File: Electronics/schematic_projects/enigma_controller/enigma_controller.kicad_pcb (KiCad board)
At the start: 6 copper layers, 156.7 x 120.8 mm, 92 parts, among them IC1 TPD8S300ARUKR, IC10 MCP23017-E_SO, IC11 RT9742SNGV, IC12 TPD1E05U06DPYT, IC13 ESD224DQAR, IC14 ESD224DQAR, IC2 ESD321DYAR, IC3 ESD321DYAR, IC4 ESD321DYAR, IC5 ESD321DYAR, IC6 ESD321DYAR, IC7 ESD321DYAR, IC8 AP22653W6-7, IC9 MCP23017-E_SO, J1 Conn_02x05_Odd_Even, J10 A70-112-331N126, J11 Conn_02x05_Odd_Even, J12 Conn_01x02, J15 Conn_01x02, J16 Conn_01x02, J17 Conn_01x02, J18 Conn_01x02, J19 Conn_01x02, J2 Conn_02x04_Odd_Even, J20 Conn_01x02, J21 Conn_02x05_Odd_Even, J22 Conn_02x05_Odd_Even, J23 Conn_01x02, J24 Conn_01x02, J25 Conn_01x02, J26 Conn_01x02, J27 Conn_01x02, J3 USB1040-GF-L-B, J4 USB_C_Receptacle_USB2.0_16P, J5 46765-0301, J6 Conn_02x05_Odd_Even, J7 Conn_02x07_Odd_Even, J8 USB3_A_Stacked, J9 Conn_02x07_Odd_Even, M1 Fan_4pin

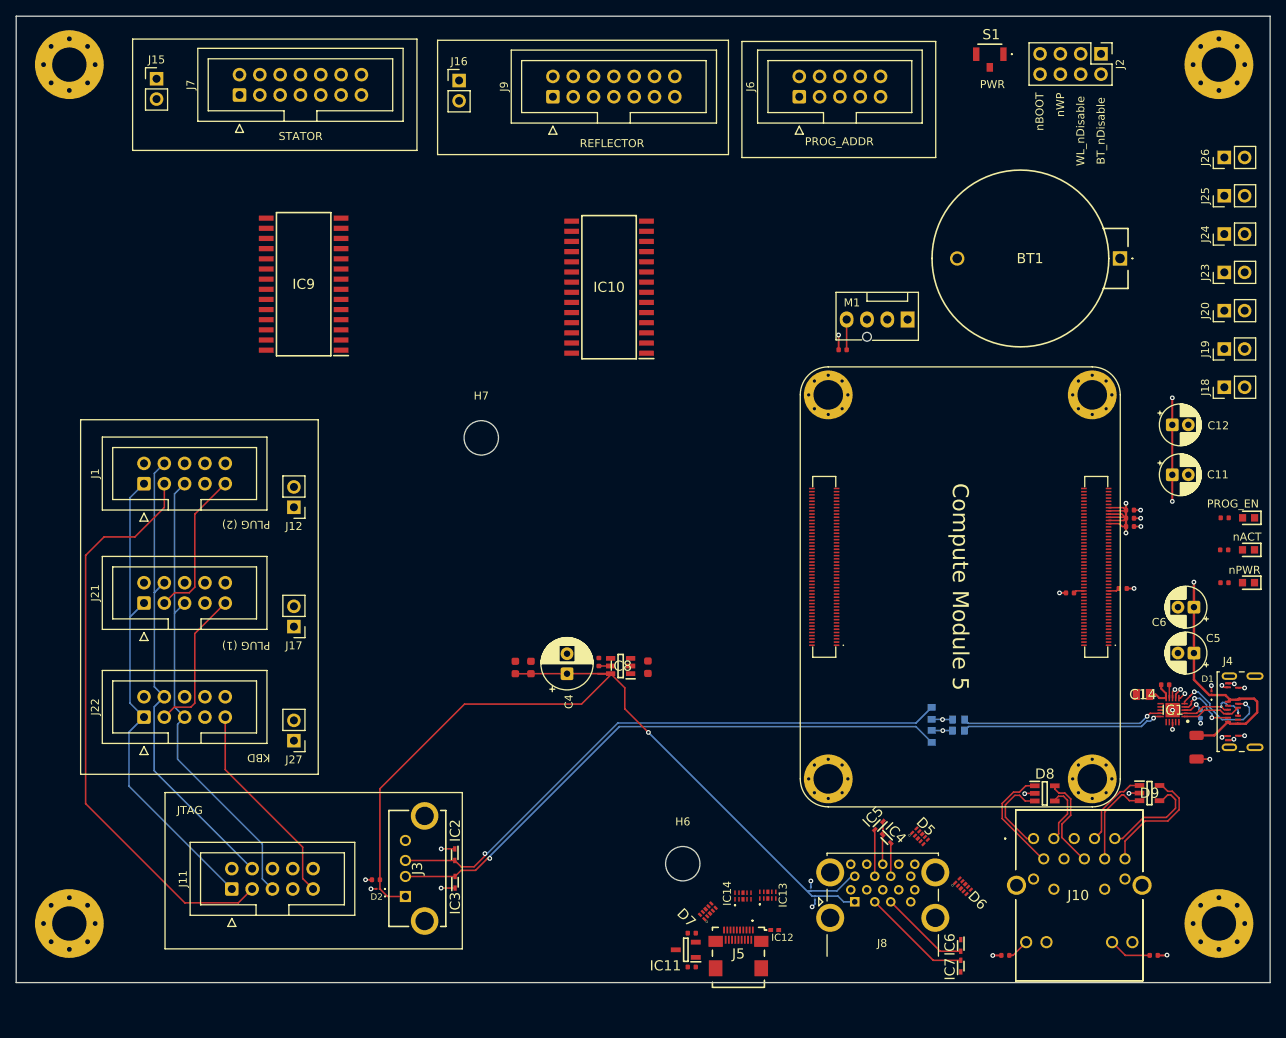
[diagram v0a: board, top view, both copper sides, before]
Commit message: Updated for impedance calculated trace widths.
Also added slow signals and traces for ESD protection components.
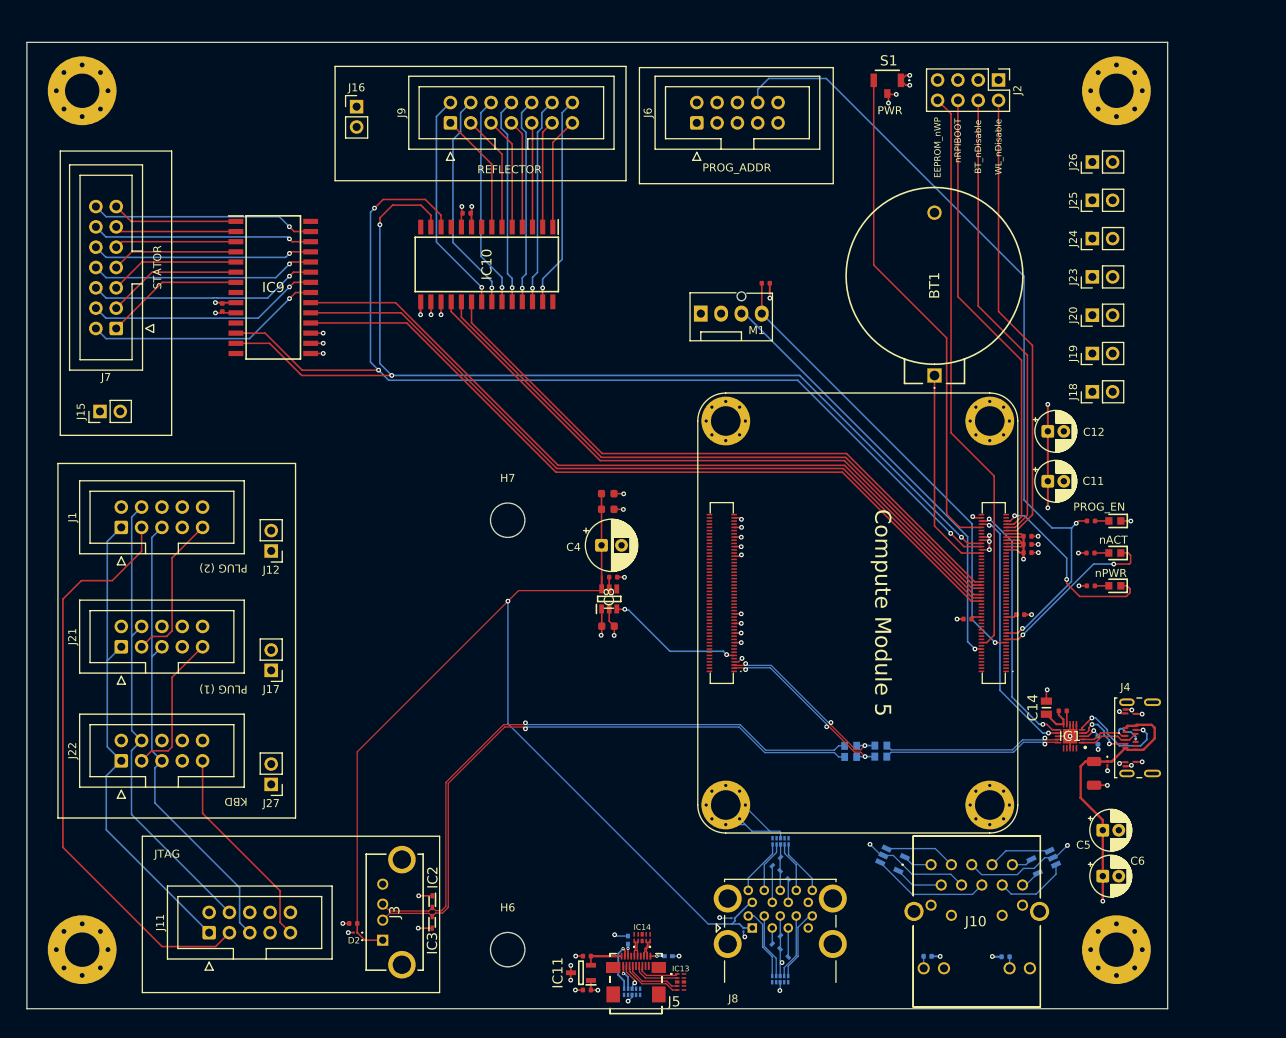
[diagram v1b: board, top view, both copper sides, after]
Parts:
- added C17: 100nF, PCM_JLCPCB:C_0402, F.Cu at (123.8, 54.2)
- added C20: 100nF, PCM_JLCPCB:C_0402, F.Cu at (93.3, 66.0)
- added IC15: TPD1E05U06DPYT, Enigma_Components:TPD1E05U06DPYT, B.Cu at (144.0, 145.1)
- D5, D6, D7, D8, D9, IC12, IC4, IC5, IC6, IC7, R3, R4: moved to B.Cu
- moved J15 42.2 mm to (78.0, 79.0), turned to 90 degrees
- moved C6 35.5 mm to (203.4, 137.1), turned to 0 degrees
- moved J7 33.0 mm to (80.1, 68.7), turned to 180 degrees
- moved BT1 27.4 mm to (182.3, 74.5), turned to -90 degrees
- moved M1 25.9 mm to (153.1, 66.8), turned to 0 degrees
- moved D6 25.6 mm to (163.1, 150.0), turned to 0 degrees
- moved C5 24.9 mm to (203.4, 131.4), turned to 0 degrees
- moved C3 24.6 mm to (141.5, 89.3), turned to 0 degrees
- moved H6 24.4 mm to (129.0, 146.3)
- moved IC7 23.3 mm to (162.6, 145.1), turned to -135 degrees
- moved IC6 22.1 mm to (163.6, 146.7), turned to -45 degrees
- moved C19 22.0 mm to (141.5, 91.2), turned to 0 degrees
- moved D8 20.8 mm to (177.1, 135.1), turned to -25 degrees
- moved R4 18.5 mm to (191.2, 147.2), turned to 180 degrees
- moved D5 17.4 mm to (163.1, 132.8), turned to 180 degrees
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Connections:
- D6 pad 1: /enigma_controller_HS/USB3_0_RX_N -> /enigma_controller_HS/USB3_0_TX_P
- D6 pad 2: /enigma_controller_HS/USB3_0_RX_P -> /enigma_controller_HS/USB3_0_TX_N
- D6 pad 4: /enigma_controller_HS/USB3_0_TX_N -> /enigma_controller_HS/USB3_0_RX_P
- D6 pad 5: /enigma_controller_HS/USB3_0_TX_P -> /enigma_controller_HS/USB3_0_RX_N
- D7 pad 1: /enigma_controller_HS/HDMI0_SDA -> /enigma_controller_HS/HDMI0_SCL
- D7 pad 2: /enigma_controller_HS/HDMI0_SCL -> /enigma_controller_HS/HDMI0_SDA
- D7 pad 4: /enigma_controller_HS/HDMI0_CEC -> unconnected-(D7-D2+-Pad4)
- D7 pad 5: /enigma_controller_HS/HDMI0_UTIL -> unconnected-(D7-D2--Pad5)
- D8 pad 1: /ETH_PAIR0_N -> /ETH_PAIR1_N
- D8 pad 3: /ETH_PAIR0_P -> /ETH_PAIR1_P
- D8 pad 4: /ETH_PAIR1_P -> /ETH_PAIR0_P
- D8 pad 5: /ETH_PAIR1_N -> /ETH_PAIR0_N
- D9 pad 4: /ETH_PAIR3_P -> /ETH_PAIR3_N
- D9 pad 5: /ETH_PAIR3_N -> /ETH_PAIR3_P
- H1 pad 46: /EXP2_INT_B -> /EXP1_nRST
- H1 pad 48: /EXP2_INT_A -> /EXP1_INT_B
- H1 pad 50: /EXP1_INT_B -> /EXP1_INT_A
- H1 pad 54: /EXP1_INT_A -> /EXP2_nRST
- H1 pad 56: /EXP2_nRST -> /EXP2_INT_B
- H1 pad 58: /EXP1_nRST -> /EXP2_INT_A
- IC10 pad 1: /pBIN_IN_B1 -> /pBIN_OUT_nOE_A
- IC10 pad 2: /pBIN_IN_B2 -> /pBIN_OUT_A6
- IC10 pad 21: /pBIN_OUT_B1 -> /pBIN_IN_B1
- IC10 pad 22: /pBIN_OUT_B2 -> /pBIN_IN_B2
- IC10 pad 23: /pBIN_OUT_B3 -> /pBIN_IN_B3
- IC10 pad 24: /pBIN_OUT_B4 -> /pBIN_IN_B4
- IC10 pad 25: /pBIN_OUT_B5 -> /pBIN_IN_B5
- IC10 pad 26: /pBIN_OUT_B6 -> /pBIN_IN_B6
- IC10 pad 27: /pBIN_OUT_nOE_B -> /pBIN_IN_nOE_B
- IC10 pad 3: /pBIN_IN_B3 -> /pBIN_OUT_A5
- IC10 pad 4: /pBIN_IN_B4 -> /pBIN_OUT_A4
- IC10 pad 5: /pBIN_IN_B5 -> /pBIN_OUT_A3
- IC10 pad 6: /pBIN_IN_B6 -> /pBIN_OUT_A2
- IC10 pad 7: /pBIN_IN_nOE_B -> /pBIN_OUT_A1
- IC13 pad 1: /enigma_controller_HS/TMDS_DATA1- -> /enigma_controller_HS/TMDS_DATA1+
- IC13 pad 2: /enigma_controller_HS/TMDS_DATA1+ -> /enigma_controller_HS/TMDS_DATA1-
- IC13 pad 4: /enigma_controller_HS/TMDS_DATA2- -> /enigma_controller_HS/TMDS_CLK+
- IC13 pad 5: /enigma_controller_HS/TMDS_DATA2+ -> /enigma_controller_HS/TMDS_CLK-
- IC14 pad 1: /enigma_controller_HS/TMDS_CLK- -> /enigma_controller_HS/TMDS_DATA0-
- IC14 pad 2: /enigma_controller_HS/TMDS_CLK+ -> /enigma_controller_HS/TMDS_DATA0+
- IC14 pad 4: /enigma_controller_HS/TMDS_DATA0- -> /enigma_controller_HS/TMDS_DATA2-
- IC14 pad 5: /enigma_controller_HS/TMDS_DATA0+ -> /enigma_controller_HS/TMDS_DATA2+
- IC9 pad 1: /pBIN_IN_A1 -> /pBIN_IN_nOE_A
- IC9 pad 2: /pBIN_IN_A2 -> /pBIN_IN_A6
- IC9 pad 21: /pBIN_OUT_A1 -> /pBIN_OUT_B1
- IC9 pad 22: /pBIN_OUT_A2 -> /pBIN_OUT_B2
- IC9 pad 23: /pBIN_OUT_A3 -> /pBIN_OUT_B3
- IC9 pad 24: /pBIN_OUT_A4 -> /pBIN_OUT_B4
- IC9 pad 25: /pBIN_OUT_A5 -> /pBIN_OUT_B5
- IC9 pad 26: /pBIN_OUT_A6 -> /pBIN_OUT_B6
- IC9 pad 27: /pBIN_OUT_nOE_A -> /pBIN_OUT_nOE_B
- IC9 pad 3: /pBIN_IN_A3 -> /pBIN_IN_A5
- IC9 pad 5: /pBIN_IN_A5 -> /pBIN_IN_A3
- IC9 pad 6: /pBIN_IN_A6 -> /pBIN_IN_A2
- IC9 pad 7: /pBIN_IN_nOE_A -> /pBIN_IN_A1
- J2 pad 2: /BT_nDisable -> /WL_nDisable
- J2 pad 4: /WL_nDisable -> /BT_nDisable
- J2 pad 6: /EEPROM_nWP -> /nRPIBOOT
- J2 pad 8: /nRPIBOOT -> /EEPROM_nWP
- J5 pad 2: /enigma_controller_HS/HDMI0_UTIL -> unconnected-(J5-UTILITY-Pad2)
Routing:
- net /I2C_SCL: track 0.00 -> 136.2 mm, vias 0 -> 3
- net /I2C_SDA: track 0.00 -> 132.9 mm, vias 0 -> 3
- net GND: track 29.0 -> 130.0 mm, vias 24 -> 58
- net /PROG_EN: track 0.00 -> 100.9 mm, vias 0 -> 2
- net /EXP1_INT_A: track 0.00 -> 99.0 mm
- net /EXP1_INT_B: track 0.00 -> 98.6 mm
- net /EXP1_nRST: track 0.00 -> 98.2 mm
- net /EXP2_nRST: track 0.00 -> 81.8 mm
- net /EXP2_INT_B: track 0.00 -> 80.8 mm
- net /EXP2_INT_A: track 0.00 -> 79.8 mm
- net /EEPROM_nWP: track 0.00 -> 71.8 mm
- net Net-(H1A-PWR_Button): track 0.00 -> 63.1 mm
- net /BT_nDisable: track 0.00 -> 57.7 mm
- net /WL_nDisable: track 0.00 -> 57.7 mm
- net /nRPIBOOT: track 0.00 -> 57.6 mm
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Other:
- board size 156.7 x 120.8 mm -> 142.6 x 120.8 mm
- board text added: "Board Stackupn [JLC06161H-1080A(Finished thickness1.57mm±10%)] L1 = Fast Signals + JTAG L2 = GND (+ SHIELD RING) L3 = +5V L4 = +3V3 L5 = GND (+ SHIELD RING) L6 = Slow Signals + JTAG"
- board text added: "EEPROM_nWP"
- board text added: "nRPIBOOT"
- board text removed: "Board Stackup L1 = Fast Signals + JTAG L2 = GND (+ SHIELD RING) L3 = +5V L4 = +3V3 L5 = GND (+ SHIELD RING) L6 = Slow Signals + JTAG"
- board text removed: "nBOOT"
- board text removed: "nWP"

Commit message: Added library from CM5IO reference design.
Updated high-speed traces with serpentines. Also added ground pour around high-speed lines.
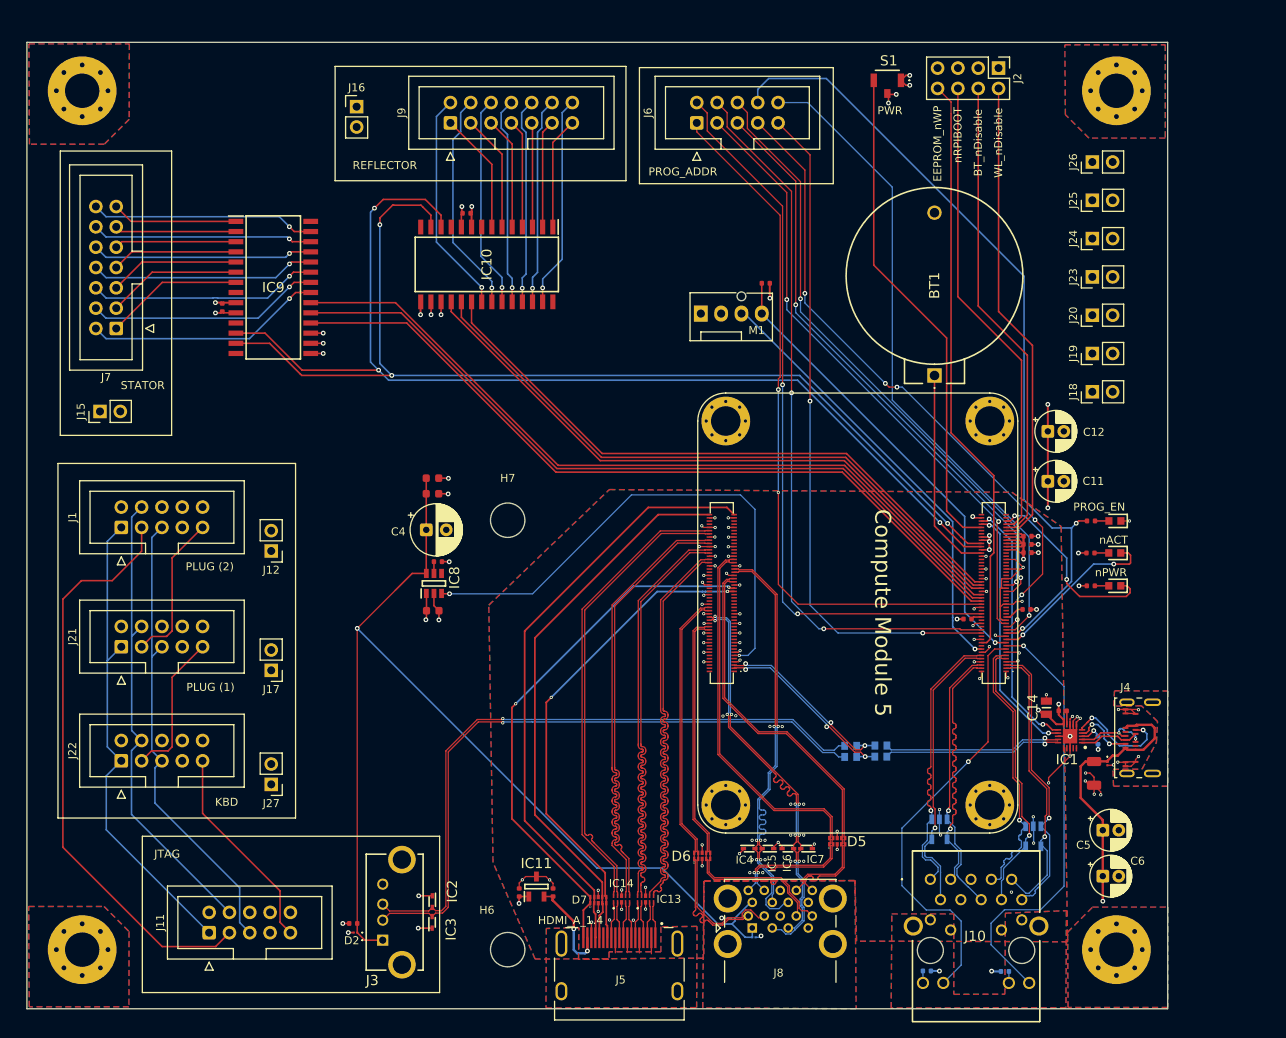
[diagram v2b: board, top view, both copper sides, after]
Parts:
- removed IC12, IC15: TPD1E05U06DPYT, Enigma_Components:TPD1E05U06DPYT
- D5, D6, D7, IC4, IC5, IC6, IC7: moved to F.Cu
- J5: value 46765-0301 -> HDMI_A_1.4; footprint Enigma_Components:467650301 -> CM5IO:EDAC 690-019-298-412
- moved C4 22.0 mm to (118.8, 93.8)
- moved C18 22.0 mm to (119.6, 103.9)
- moved C19 22.0 mm to (119.6, 89.3)
- moved C3 22.0 mm to (119.6, 87.4)
- moved IC8 22.0 mm to (119.8, 100.5)
- moved R9 22.0 mm to (120.3, 97.8)
- moved D6 18.2 mm to (153.3, 134.6)
- moved C7 14.8 mm to (130.4, 139.2), turned to 90 degrees
- moved IC6 13.0 mm to (164.0, 133.7), turned to 0 degrees
- moved D7 12.2 mm to (140.3, 140.1)
- moved IC11 12.1 mm to (132.6, 138.4), turned to 90 degrees
- moved IC7 12.0 mm to (166.3, 133.7), turned to 180 degrees
- moved IC13 11.3 mm to (146.2, 140.0), turned to 90 degrees
- moved C8 9.02 mm to (134.7, 139.2), turned to 90 degrees
- moved D5 7.08 mm to (170.2, 132.7), turned to 0 degrees
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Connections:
- net /enigma_controller_HS/USB3_0_DM renamed /enigma_controller_HS/USB3_0_DN
- net /enigma_controller_HS/USB3_1_DM renamed /enigma_controller_HS/USB3_1_DN
- D5 pad 1: /enigma_controller_HS/USB3_1_RX_N -> /enigma_controller_HS/USB3_1_TX_P
- D5 pad 10: unconnected-(D5-NC_4-Pad10) -> /enigma_controller_HS/USB3_1_TX_P
- D5 pad 2: /enigma_controller_HS/USB3_1_RX_P -> /enigma_controller_HS/USB3_1_TX_N
- D5 pad 4: /enigma_controller_HS/USB3_1_TX_N -> /enigma_controller_HS/USB3_1_RX_P
- D5 pad 5: /enigma_controller_HS/USB3_1_TX_P -> /enigma_controller_HS/USB3_1_RX_N
- D5 pad 6: unconnected-(D5-NC_1-Pad6) -> /enigma_controller_HS/USB3_1_RX_N
- D5 pad 7: unconnected-(D5-NC_2-Pad7) -> /enigma_controller_HS/USB3_1_RX_P
- D5 pad 9: unconnected-(D5-NC_3-Pad9) -> /enigma_controller_HS/USB3_1_TX_N
- D6 pad 10: unconnected-(D6-NC_4-Pad10) -> /enigma_controller_HS/USB3_0_TX_P
- D6 pad 6: unconnected-(D6-NC_1-Pad6) -> /enigma_controller_HS/USB3_0_RX_N
- D6 pad 7: unconnected-(D6-NC_2-Pad7) -> /enigma_controller_HS/USB3_0_RX_P
- D6 pad 9: unconnected-(D6-NC_3-Pad9) -> /enigma_controller_HS/USB3_0_TX_N
- D7 pad 1: /enigma_controller_HS/HDMI0_SCL -> /enigma_controller_HS/HDMI0_HOT_PLUG
- D7 pad 10: unconnected-(D7-NC_4-Pad10) -> /enigma_controller_HS/HDMI0_HOT_PLUG
- D7 pad 4: unconnected-(D7-D2+-Pad4) -> /enigma_controller_HS/HDMI0_SCL
- D7 pad 5: unconnected-(D7-D2--Pad5) -> /enigma_controller_HS/HDMI0_CEC
- D7 pad 6: unconnected-(D7-NC_1-Pad6) -> /enigma_controller_HS/HDMI0_CEC
- D7 pad 7: unconnected-(D7-NC_2-Pad7) -> /enigma_controller_HS/HDMI0_SCL
- D7 pad 9: unconnected-(D7-NC_3-Pad9) -> /enigma_controller_HS/HDMI0_SDA
- D8 pad 1: /ETH_PAIR1_N -> /ETH_PAIR0_P
- D8 pad 3: /ETH_PAIR1_P -> /ETH_PAIR1_N
- D8 pad 4: /ETH_PAIR0_P -> /ETH_PAIR1_P
- D9 pad 3: /ETH_PAIR2_N -> /ETH_PAIR3_N
- D9 pad 4: /ETH_PAIR3_N -> /ETH_PAIR3_P
- D9 pad 5: /ETH_PAIR3_P -> /ETH_PAIR2_N
- IC13 pad 1: /enigma_controller_HS/TMDS_DATA1+ -> /enigma_controller_HS/TMDS_DATA1-
- IC13 pad 2: /enigma_controller_HS/TMDS_DATA1- -> /enigma_controller_HS/TMDS_DATA1+
- IC13 pad 4: /enigma_controller_HS/TMDS_CLK+ -> /enigma_controller_HS/TMDS_DATA2-
- IC13 pad 5: /enigma_controller_HS/TMDS_CLK- -> /enigma_controller_HS/TMDS_DATA2+
- IC14 pad 1: /enigma_controller_HS/TMDS_DATA0- -> /enigma_controller_HS/TMDS_CLK-
- IC14 pad 2: /enigma_controller_HS/TMDS_DATA0+ -> /enigma_controller_HS/TMDS_CLK+
- IC14 pad 4: /enigma_controller_HS/TMDS_DATA2- -> /enigma_controller_HS/TMDS_DATA0-
- IC14 pad 5: /enigma_controller_HS/TMDS_DATA2+ -> /enigma_controller_HS/TMDS_DATA0+
- J5 pad 1: /enigma_controller_HS/HDMI0_HOT_PLUG -> /enigma_controller_HS/TMDS_DATA2+
- J5 pad 10: /SHIELD -> /enigma_controller_HS/TMDS_CLK+
- J5 pad 11: /enigma_controller_HS/TMDS_DATA0- -> /SHIELD
- J5 pad 12: /enigma_controller_HS/TMDS_CLK+ -> /enigma_controller_HS/TMDS_CLK-
- J5 pad 13: /SHIELD -> /enigma_controller_HS/HDMI0_CEC
- J5 pad 14: /enigma_controller_HS/TMDS_CLK- -> unconnected-(J5-UTILITY/HEAC+-Pad14)
- J5 pad 15: /enigma_controller_HS/HDMI0_CEC -> /enigma_controller_HS/HDMI0_SCL
- J5 pad 16: GND -> /enigma_controller_HS/HDMI0_SDA
- J5 pad 17: /enigma_controller_HS/HDMI0_SCL -> GND
- J5 pad 18: /enigma_controller_HS/HDMI0_SDA -> /enigma_controller_HS/HDMI_5V
- J5 pad 19: /enigma_controller_HS/HDMI_5V -> /enigma_controller_HS/HDMI0_HOT_PLUG
- J5 pad 2: unconnected-(J5-UTILITY-Pad2) -> /SHIELD
- J5 pad 3: /enigma_controller_HS/TMDS_DATA2+ -> /enigma_controller_HS/TMDS_DATA2-
- J5 pad 4: /SHIELD -> /enigma_controller_HS/TMDS_DATA1+
- J5 pad 5: /enigma_controller_HS/TMDS_DATA2- -> /SHIELD
- J5 pad 6: /enigma_controller_HS/TMDS_DATA1+ -> /enigma_controller_HS/TMDS_DATA1-
- J5 pad 7: /SHIELD -> /enigma_controller_HS/TMDS_DATA0+
- J5 pad 8: /enigma_controller_HS/TMDS_DATA1- -> /SHIELD
- J5 pad 9: /enigma_controller_HS/TMDS_DATA0+ -> /enigma_controller_HS/TMDS_DATA0-
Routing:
- net /MAP_ADDR_2: track 0.00 -> 92.3 mm, vias 0 -> 2
- net /MAP_ADDR_4: track 0.00 -> 91.4 mm, vias 0 -> 2
- net /MAP_ADDR_1: track 0.00 -> 88.5 mm, vias 0 -> 2
- net /PROG_nWE_A: track 0.00 -> 84.8 mm, vias 0 -> 2
- net /PROG_nWE_B: track 0.00 -> 82.9 mm, vias 0 -> 1
- net /MAP_ADDR_7: track 0.00 -> 80.9 mm, vias 0 -> 6
- net /MAP_ADDR_3: track 0.00 -> 78.0 mm, vias 0 -> 2
- net /MAP_ADDR_6: track 0.00 -> 77.0 mm, vias 0 -> 2
- net /MAP_ADDR_5: track 0.00 -> 73.3 mm, vias 0 -> 2
- net /enigma_controller_HS/HDMI0_SDA: track 3.18 -> 75.1 mm, vias 1 -> 0
- net /enigma_controller_HS/HDMI0_HOT_PLUG: track 1.75 -> 67.3 mm, vias 1 -> 2
- net /enigma_controller_HS/HDMI0_SCL: track 6.58 -> 69.4 mm, vias 1 -> 0
- net /enigma_controller_HS/HDMI0_CEC: track 1.52 -> 61.8 mm, vias 1 -> 2
- net /enigma_controller_HS/HDMI0_CLK_N: track 0.00 -> 57.5 mm
- net /enigma_controller_HS/HDMI0_CLK_P: track 0.00 -> 57.5 mm
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- added copper zone on B.Cu, net /SHIELD
- added copper zone on F.Cu, net /SHIELD
- added copper zone on In1.Cu, net /SHIELD
- added copper zone on In2.Cu, net /SHIELD
- added copper zone on In3.Cu, net /SHIELD
- added copper zone on B.Cu, net GND
- added copper zone on F.Cu, net GND
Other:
- board text removed: "Board Stackupn [JLC06161H-1080A(Finished thickness1.57mm±10%)] L1 = Fast Signals + JTAG L2 = GND (+ SHIELD RING) L3 = +5V L4 = +3V3 L5 = GND (+ SHIELD RING) L6 = Slow Signals + JTAG"

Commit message: Updated for new battery holder.
Also updated 3d models for components and fixed skew and trace lengths for main high-speed lines.
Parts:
- removed R11, R12, R13, R14: RCA06030000ZSEA, Enigma_Components:RESC1608X50N
- BT1: value BS-02-A1AJ006 -> CR2032-BS-6-1; footprint Enigma_Components:BS02A1AJ006 -> Enigma_Components:CR2032BS61
- C15, D8, D9: moved to F.Cu
- moved BT1 15.3 mm to (184.7, 59.4), turned to 90 degrees
- moved J18 3.23 mm to (205.3, 76.5)
- moved J19 3.23 mm to (205.3, 71.8)
- moved J20 3.23 mm to (205.3, 67.0)
- moved J23 3.23 mm to (205.3, 62.2)
- moved J24 3.23 mm to (205.3, 57.4)
- moved J25 3.23 mm to (205.3, 52.6)
- moved J26 3.23 mm to (205.3, 47.8)
- moved D8 2.06 mm to (182.7, 129.2)
- moved C15 1.70 mm to (203.4, 118.5), turned to 180 degrees
- moved R5 1.66 mm to (198.4, 114.8)
- moved D9 0.91 mm to (195.5, 131.6)
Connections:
- D8 pad 1: /ETH_PAIR0_P -> /ETH_PAIR1_N
- D8 pad 3: /ETH_PAIR1_N -> /ETH_PAIR0_N
- D8 pad 4: /ETH_PAIR1_P -> /ETH_PAIR0_P
- D8 pad 5: /ETH_PAIR0_N -> /ETH_PAIR1_P
- D9 pad 1: /ETH_PAIR2_P -> /ETH_PAIR3_P
- D9 pad 3: /ETH_PAIR3_N -> /ETH_PAIR2_N
- D9 pad 4: /ETH_PAIR3_P -> /ETH_PAIR2_P
- D9 pad 5: /ETH_PAIR2_N -> /ETH_PAIR3_N
- H1 pad 103: /USB_DN -> /JTAG_USB_N
- H1 pad 105: /USB_DP -> /JTAG_USB_P
- IC1 pad 1: /C_D+ -> unconnected-(IC1-C_SBU1-Pad1)
- IC1 pad 14: /FLASH_D+ -> unconnected-(IC1-SBU2-Pad14)
- IC1 pad 15: /FLASH_D- -> unconnected-(IC1-SBU1-Pad15)
- IC1 pad 2: /C_D- -> unconnected-(IC1-C_SBU2-Pad2)
- J4 pad A6: /C_D+ -> unconnected-(J4-D+-PadA6)
- J4 pad A7: /C_D- -> unconnected-(J4-D--PadA7)
- J4 pad B6: /C_D+ -> unconnected-(J4-D+-PadB6)
- J4 pad B7: /C_D- -> unconnected-(J4-D--PadB7)
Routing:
- net /USB_DN: track 23.7 -> 0.00 mm, vias 3 -> 0
- net /USB_DP: track 23.6 -> 0.00 mm, vias 3 -> 0
- net /FLASH_D-: track 22.4 -> 0.00 mm, vias 1 -> 0
- net /FLASH_D+: track 22.3 -> 0.00 mm, vias 1 -> 0
- net Net-(BT1-+): track 26.1 -> 46.2 mm
- net /JTAG_USB_P: track 81.6 -> 66.1 mm, vias 1 -> 2
- net /JTAG_USB_N: track 81.6 -> 66.1 mm, vias 1 -> 2
- net /C_D-: track 9.54 -> 0.00 mm, vias 2 -> 0
- net /C_D+: track 7.55 -> 0.00 mm
- net /C_CC2: track 13.3 -> 7.28 mm
- net /ETH_LED_nAct: track 53.7 -> 57.8 mm
- net /ETH_PAIR1_N: track 34.1 -> 38.2 mm
- net /ETH_PAIR1_P: track 33.8 -> 37.9 mm
- net /ETH_PAIR2_N: track 34.6 -> 38.5 mm
- net /ETH_PAIR2_P: track 34.5 -> 38.3 mm
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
